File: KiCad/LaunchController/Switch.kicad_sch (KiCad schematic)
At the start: 41 parts, among them U5 U74HC14

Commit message: 圧力センサとの接続部を追加
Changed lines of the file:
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@@
-    (effects (font (size 1.27 1.27)) (justify left bottom))
-  )
-  (text "PURGE SWITCH\nA ALT PU" (at 95.25 170.18 0)
     (effects (font (size 1.27 1.27)) (justify left bottom))
   )

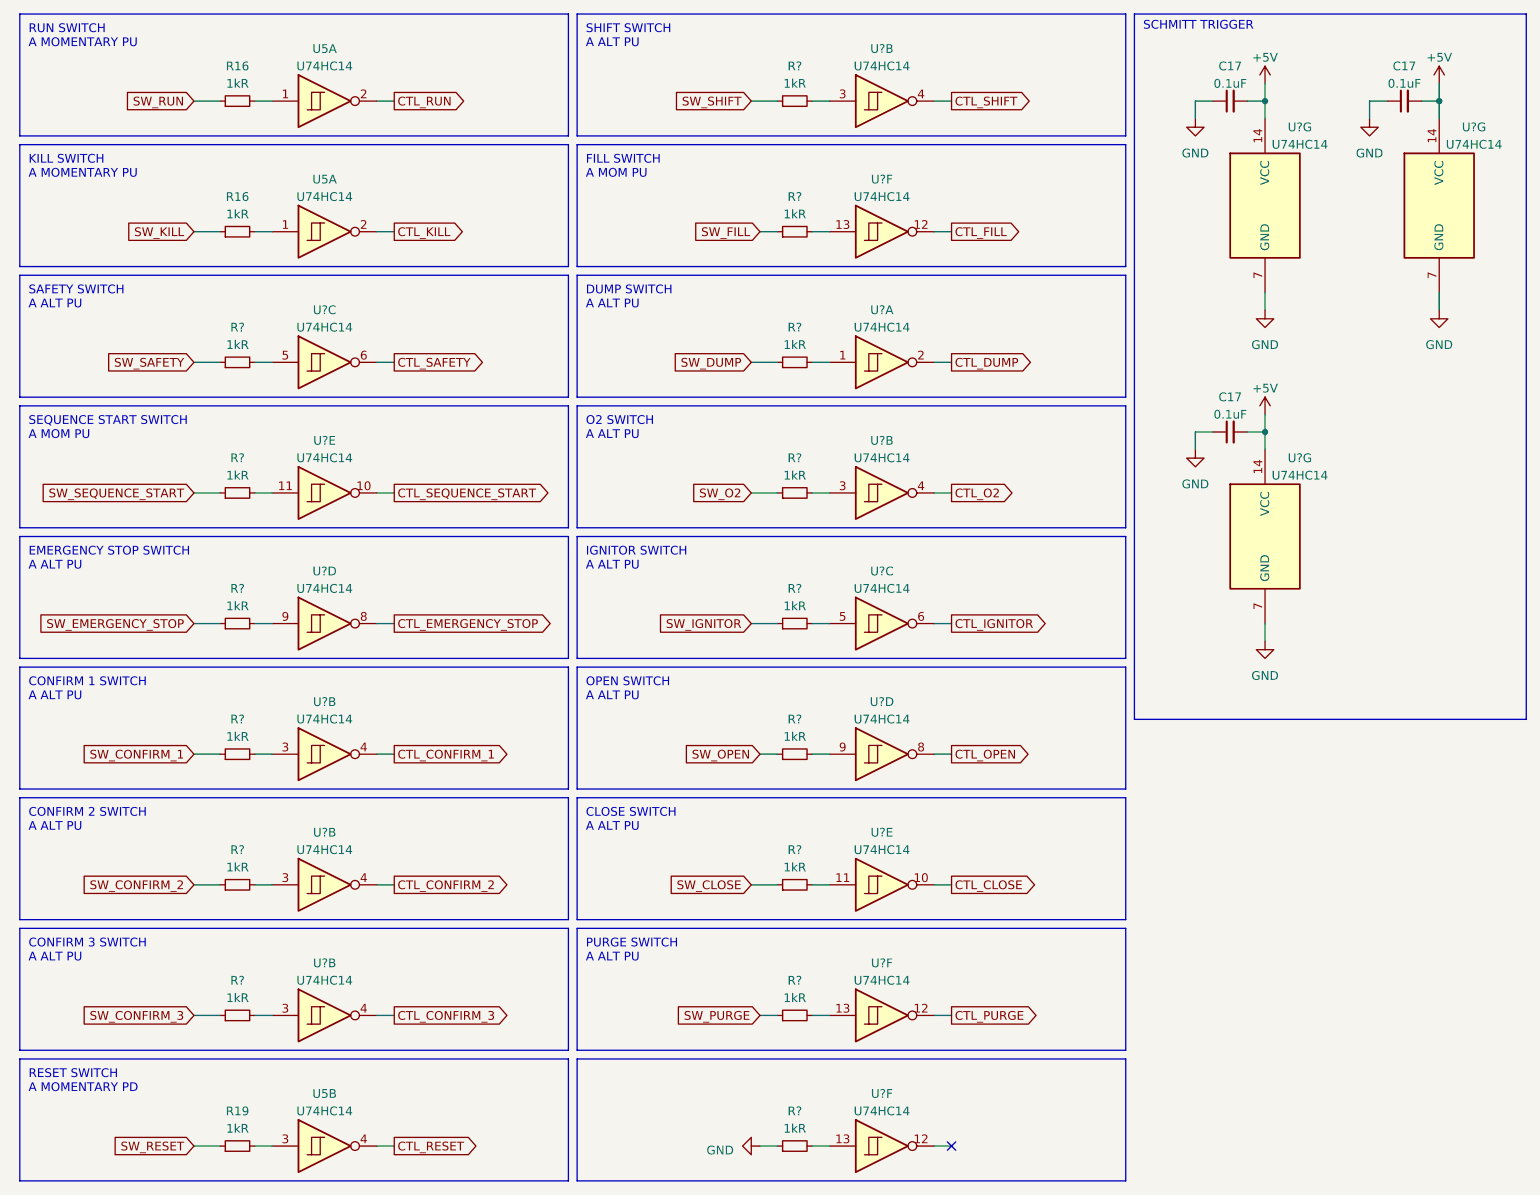
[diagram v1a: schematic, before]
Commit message: ジャンパーを回路図に追加
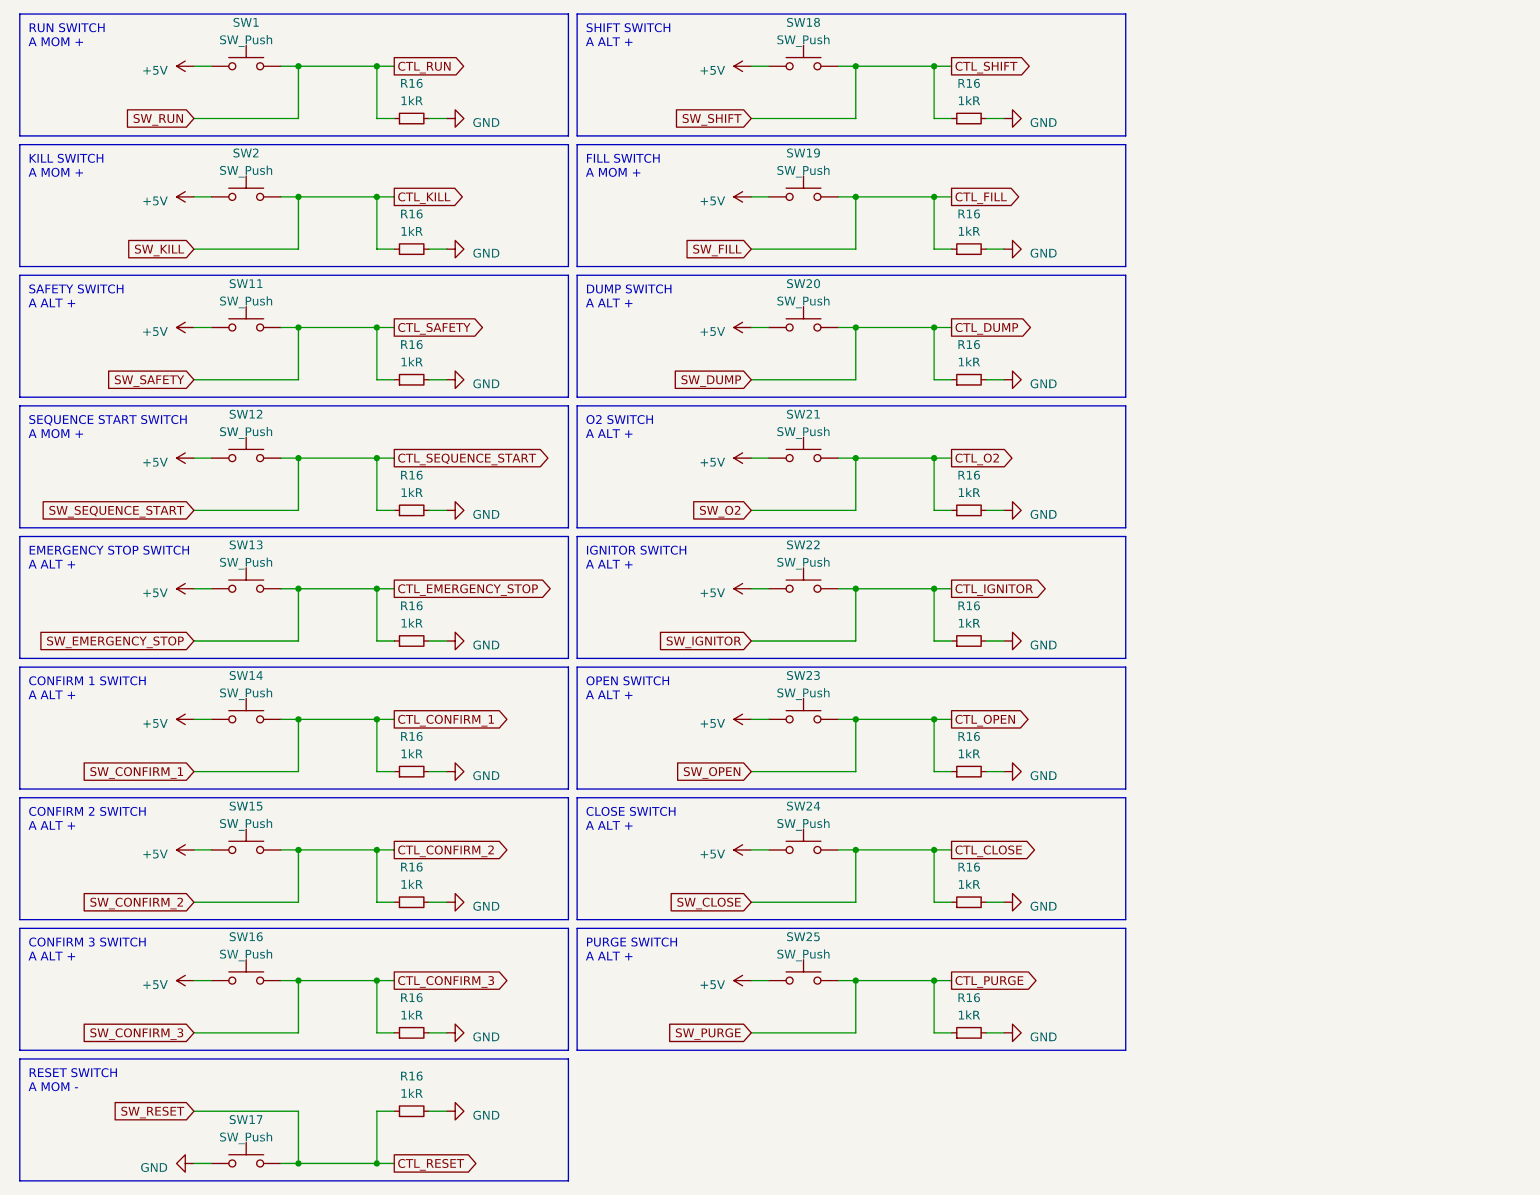
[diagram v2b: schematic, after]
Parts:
- removed C17 (x3): 0.1uF, Capacitor_SMD:C_0603_1608Metric_Pad1.08x0.95mm_HandSolder, symbol Device:C_Small
- removed R16, R19, R? (x15): 1kR, Resistor_SMD:R_0603_1608Metric_Pad0.98x0.95mm_HandSolder, symbol Device:R_Small
- removed U5, U? (x18): U74HC14, Package_SO:TSSOP-14_4.4x5mm_P0.65mm, symbol 74xx:74HC14
- added R16 (x16): 1kR, Resistor_SMD:R_0603_1608Metric_Pad0.98x0.95mm_HandSolder, symbol Device:R_Small
- added SW1, SW11, SW12, SW13, SW14, SW15, SW16, SW17, SW18, SW19, SW2, SW20, SW21, SW22, SW23, SW24, SW25: SW_Push, Connector_PinHeader_2.54mm:PinHeader_1x02_P2.54mm_Vertical, symbol Switch:SW_Push
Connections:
- net SW_RUN is gone; now on net CTL_RUN: R16.1
- net +5V: now also SW1.1, SW11.1, SW12.1, SW13.1, SW14.1, SW15.1, SW16.1, SW18.1, SW19.1, SW2.1, SW20.1, SW21.1, SW22.1, SW23.1, SW24.1, SW25.1
- net CTL_CLOSE: now also R16.1, SW24.2
- net CTL_CONFIRM_1: now also R16.1, SW14.2
- net CTL_CONFIRM_2: now also R16.1, SW15.2
- net CTL_CONFIRM_3: now also R16.1, SW16.2
- net CTL_DUMP: now also R16.1, SW20.2
- net CTL_EMERGENCY_STOP: now also R16.1, SW13.2
- net CTL_FILL: now also R16.1, SW19.2
- net CTL_IGNITOR: now also R16.1, SW22.2
- net CTL_KILL: now also R16.1, SW2.2
- net CTL_O2: now also R16.1, SW21.2
- net CTL_OPEN: now also R16.1, SW23.2
- net CTL_PURGE: now also R16.1, SW25.2
- net CTL_RESET: now also R16.1, SW17.2
- net CTL_RUN: now also SW1.2
- net CTL_SAFETY: now also R16.1, SW11.2
- net CTL_SEQUENCE_START: now also R16.1, SW12.2
- net CTL_SHIFT: now also R16.1, SW18.2
- net GND: now also R16.2, R16.2, R16.2, R16.2, R16.2, R16.2, R16.2, R16.2, R16.2, R16.2, R16.2, R16.2, R16.2, R16.2, R16.2, R16.2, R16.2, SW17.1
- no-connect marks 1 -> 0
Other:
- note added: "CLOSE SWITCH A ALT +"
- note added: "CONFIRM 1 SWITCH A ALT +"
- note added: "CONFIRM 2 SWITCH A ALT +"
- note added: "CONFIRM 3 SWITCH A ALT +"
- note added: "DUMP SWITCH A ALT +"
- note added: "EMERGENCY STOP SWITCH A ALT +"
- note added: "FILL SWITCH A MOM +"
- note added: "IGNITOR SWITCH A ALT +"
- note added: "KILL SWITCH A MOM +"
- note added: "O2 SWITCH A ALT +"
- note added: "OPEN SWITCH A ALT +"
- note added: "PURGE SWITCH A ALT +"
- note added: "RESET SWITCH A MOM -"
- note added: "RUN SWITCH A MOM +"
- note added: "SAFETY SWITCH A ALT +"
- note added: "SEQUENCE START SWITCH A MOM +"
- note added: "SHIFT SWITCH A ALT +"
- note removed: "CLOSE SWITCH A ALT PU"
- note removed: "CONFIRM 1 SWITCH A ALT PU"
- note removed: "CONFIRM 2 SWITCH A ALT PU"
- note removed: "CONFIRM 3 SWITCH A ALT PU"
- note removed: "DUMP SWITCH A ALT PU"
- note removed: "EMERGENCY STOP SWITCH A ALT PU"
- note removed: "FILL SWITCH A MOM PU"
- note removed: "IGNITOR SWITCH A ALT PU"
- note removed: "KILL SWITCH A MOMENTARY PU"
- note removed: "O2 SWITCH A ALT PU"
- note removed: "OPEN SWITCH A ALT PU"
- note removed: "PURGE SWITCH A ALT PU"
- note removed: "RESET SWITCH A MOMENTARY PD"
- note removed: "RUN SWITCH A MOMENTARY PU"
- note removed: "SAFETY SWITCH A ALT PU"
- note removed: "SCHMITT TRIGGER"
- note removed: "SEQUENCE START SWITCH A MOM PU"
- note removed: "SHIFT SWITCH A ALT PU"
- moved on the sheet: R16

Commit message: ランコンおわり
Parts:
- removed R16: 1kR, Resistor_SMD:R_0603_1608Metric_Pad0.98x0.95mm_HandSolder, symbol Device:R_Small
- SW1, SW17, SW2: footprint Connector_PinHeader_2.54mm:PinHeader_1x02_P2.54mm_Vertical -> TSRP_Button_Switch_SMD:TVAF06-A020B-R
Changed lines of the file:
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@@
   (junction (at 134.62 77.47) (diameter 0) (color 0 0 0 0)
   )
-  (junction (at 64.77 180.34) (diameter 0) (color 0 0 0 0)
-  )
   (junction (at 53.34 180.34) (diameter 0) (color 0 0 0 0)
   )
@@
     (stroke (width 0) (type default))
   )
-  (wire (pts (xy 72.39 172.72) (xy 74.93 172.72))
-    (stroke (width 0) (type default))
-  )
   (wire (pts (xy 132.08 134.62) (xy 134.62 134.62))
     (stroke (width 0) (type default))
@@
     (stroke (width 0) (type default))
   )
-  (wire (pts (xy 64.77 180.34) (xy 67.31 180.34))
-    (stroke (width 0) (type default))
-  )
   (wire (pts (xy 134.62 77.47) (xy 146.05 77.47))
     (stroke (width 0) (type default))
@@
     (stroke (width 0) (type default))
   )
-  (wire (pts (xy 53.34 180.34) (xy 64.77 180.34))
+  (wire (pts (xy 53.34 180.34) (xy 67.31 180.34))
     (stroke (width 0) (type default))
   )
@@
     (stroke (width 0) (type default))
   )
-  (wire (pts (xy 64.77 172.72) (xy 64.77 180.34))
-    (stroke (width 0) (type default))
-  )
   (wire (pts (xy 72.39 104.14) (xy 74.93 104.14))
     (stroke (width 0) (type default))
@@
   )
   (wire (pts (xy 38.1 172.72) (xy 53.34 172.72))
-    (stroke (width 0) (type default))
-  )
-  (wire (pts (xy 67.31 172.72) (xy 64.77 172.72))
     (stroke (width 0) (type default))
   )
@@
       (effects (font (size 1.27 1.27)))
     )
-    (property "Footprint" "Connector_PinHeader_2.54mm:PinHeader_1x02_P2.54mm_Vertical" (at 45.72 34.29 0)
-      (effects (font (size 1.27 1.27)) hide)
-    )
-    (property "Datasheet" "https://akizukidenshi.com/catalog/g/gC-08593/" (at 45.72 34.29 0)
+    (property "Footprint" "TSRP_Button_Switch_SMD:TVAF06-A020B-R" (at 45.72 34.29 0)
+      (effects (font (size 1.27 1.27)) hide)
+    )
+    (property "Datasheet" "https://akizukidenshi.com/catalog/g/gP-14888/" (at 45.72 34.29 0)
       (effects (font (size 1.27 1.27)) hide)
     )
@@
       (effects (font (size 1.27 1.27)))
     )
-    (property "Footprint" "Connector_PinHeader_2.54mm:PinHeader_1x02_P2.54mm_Vertical" (at 45.72 15.24 0)
-      (effects (font (size 1.27 1.27)) hide)
-    )
-    (property "Datasheet" "https://akizukidenshi.com/catalog/g/gC-08593/" (at 45.72 15.24 0)
+    (property "Footprint" "TSRP_Button_Switch_SMD:TVAF06-A020B-R" (at 45.72 15.24 0)
+      (effects (font (size 1.27 1.27)) hide)
+    )
+    (property "Datasheet" "https://akizukidenshi.com/catalog/g/gP-14888/" (at 45.72 15.24 0)
       (effects (font (size 1.27 1.27)) hide)
     )
@@
     )
   )
-  (symbol (lib_id "Device:R_Small") (at 69.85 172.72 90) (unit 1)
-    (in_bom yes) (on_board yes) (dnp no)
-    (property "Reference" "R16" (at 69.85 167.64 90)
-      (effects (font (size 1.27 1.27)))
-    )
-    (property "Value" "1kR" (at 69.85 170.18 90)
-      (effects (font (size 1.27 1.27)))
-    )
-    (property "Footprint" "Resistor_SMD:R_0603_1608Metric_Pad0.98x0.95mm_HandSolder" (at 69.85 172.72 0)
-      (effects (font (size 1.27 1.27)) hide)
-    )
-    (property "Datasheet" "https://www.chip1stop.com/view/dispDetail/DispDetail?partId=ROHM-0021097" (at 69.85 172.72 0)
-      (effects (font (size 1.27 1.27)) hide)
-    )
-    (property "LCSC" "" (at 69.85 172.72 0)
-      (effects (font (size 1.27 1.27)) hide)
-    )
-    (pin "1")
-    (pin "2")
-    (instances
-      (project "LaunchController"
-        (path "/628d040b-43bf-4733-804f-091644a90124"
-          (reference "R16") (unit 1)
-        )
-        (path "/628d040b-43bf-4733-804f-091644a90124/50cfa140-fcaf-4528-b6e7-da7a529677fd"
-          (reference "R58") (unit 1)
-        )
-      )
-      (project "Switch"
-        (path "/7a9db562-9ba2-4e28-86d0-8020190b3bce"
-          (reference "R16") (unit 1)
-        )
-      )
-    )
-  )
   (symbol (lib_id "power:GND") (at 156.21 46.99 90) (unit 1)
     (in_bom yes) (on_board yes) (dnp no) (fields_autoplaced)
@@
       (effects (font (size 1.27 1.27)))
     )
-    (property "Footprint" "Connector_PinHeader_2.54mm:PinHeader_1x02_P2.54mm_Vertical" (at 45.72 175.26 0)
-      (effects (font (size 1.27 1.27)) hide)
-    )
-    (property "Datasheet" "https://akizukidenshi.com/catalog/g/gC-08593/" (at 45.72 175.26 0)
+    (property "Footprint" "TSRP_Button_Switch_SMD:TVAF06-A020B-R" (at 45.72 175.26 0)
+      (effects (font (size 1.27 1.27)) hide)
+    )
+    (property "Datasheet" "https://akizukidenshi.com/catalog/g/gP-14888/" (at 45.72 175.26 0)
       (effects (font (size 1.27 1.27)) hide)
     )
@@
         )
       )
-    )
-  )
-  (symbol (lib_id "power:GND") (at 74.93 172.72 90) (unit 1)
-    (in_bom yes) (on_board yes) (dnp no) (fields_autoplaced)
-    (property "Reference" "#PWR0118" (at 81.28 172.72 0)
-      (effects (font (size 1.27 1.27)) hide)
-    )
-    (property "Value" "GND" (at 78.74 173.355 90)
-      (effects (font (size 1.27 1.27)) (justify right))
-    )
-    (property "Footprint" "" (at 74.93 172.72 0)
-      (effects (font (size 1.27 1.27)) hide)
-    )
-    (property "Datasheet" "" (at 74.93 172.72 0)
-      (effects (font (size 1.27 1.27)) hide)
-    )
-    (pin "1")
-    (instances
-      (project "LaunchController"
-        (path "/628d040b-43bf-4733-804f-091644a90124/50cfa140-fcaf-4528-b6e7-da7a529677fd"
-          (reference "#PWR0118") (unit 1)
-        )
-      )
